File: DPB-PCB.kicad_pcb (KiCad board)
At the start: 4 copper layers, 86.6 x 60 mm, 98 parts, among them J1 USB_C_Prog, J2 LCD_Conn, J3 IMU_FFC_Conn, J4 IR_SENSOR, J5 ESC_Conn, J6 IR_LED, J7 XT60 - M, J8 USB_C_OTG, Q1 AO3401A, Q2 MMBT5551, Q3 MMBT5551, U1 ESP32-S3-WROOM-1-N4R2, U2 RT7272BGSP, U3 AMS1117-3.3, U4 USBLC6-4SC6, U5 CP2102N-Axx-xQFN28, U6 USBLC6-4SC6, U7 LM358

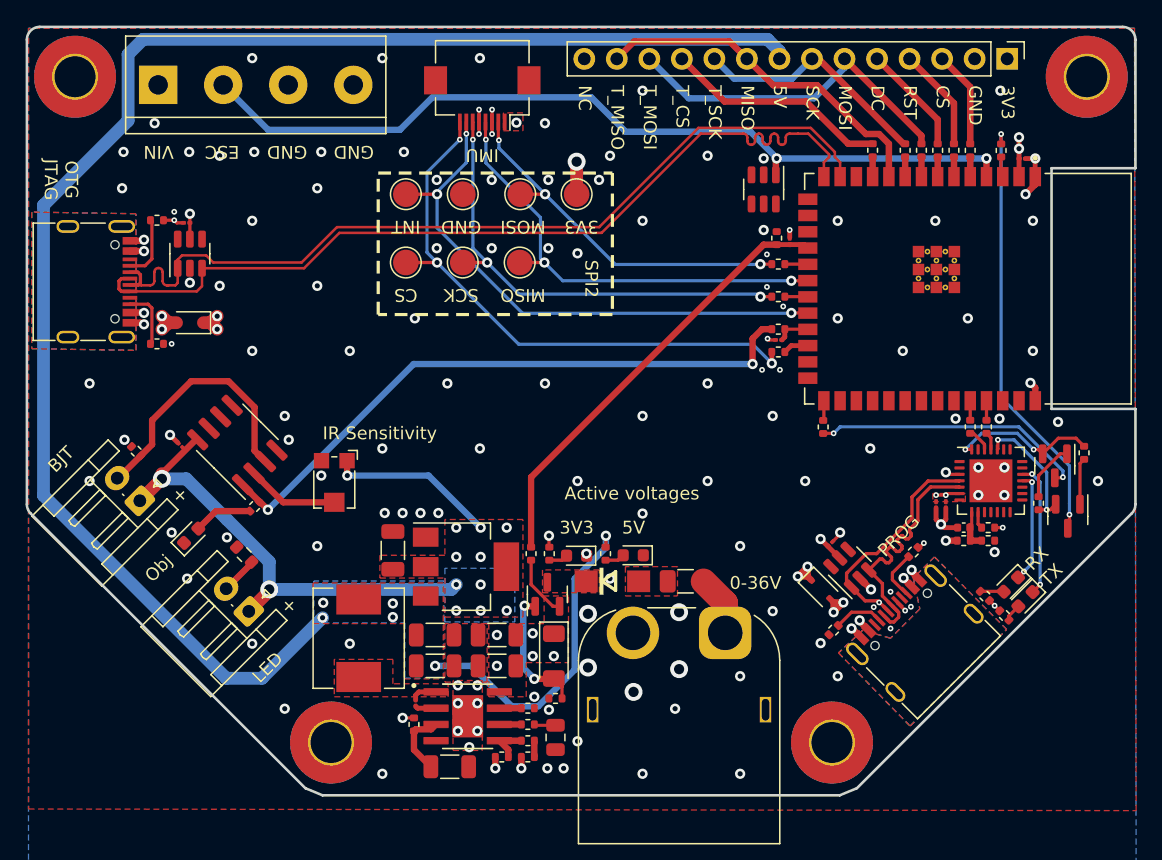
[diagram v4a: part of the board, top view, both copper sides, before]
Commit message: Align mech holed
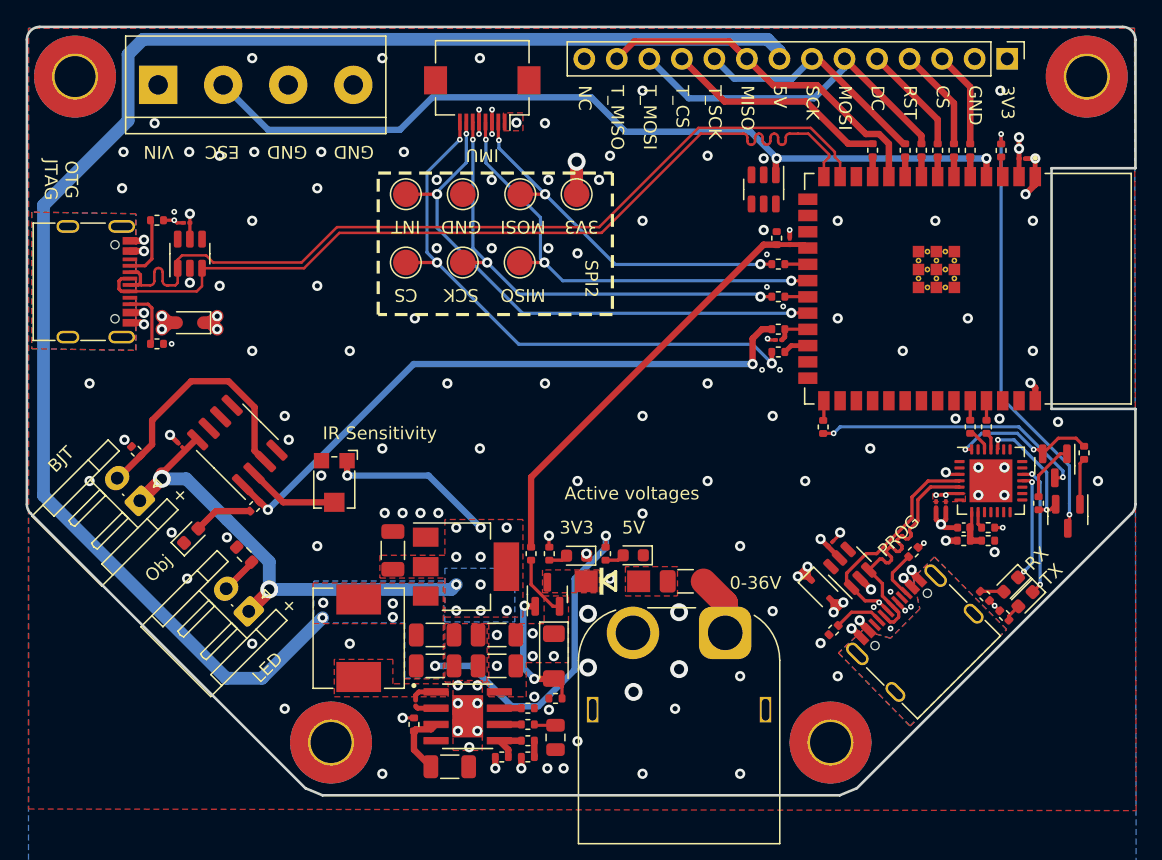
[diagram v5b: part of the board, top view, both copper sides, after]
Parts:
- moved H2 0.12 mm to (163.0, 134.0)
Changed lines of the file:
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@@
       (layer "F.SilkS" (type "Top Silk Screen") (color "White"))
       (layer "F.Paste" (type "Top Solder Paste"))
-      (layer "F.Mask" (type "Top Solder Mask") (color "Black") (thickness 0.01))
+      (layer "F.Mask" (type "Top Solder Mask") (color "Blue") (thickness 0.01))
       (layer "F.Cu" (type "copper") (thickness 0.035))
-      (layer "dielectric 1" (type "prepreg") (thickness 0.2104) (material "FR4") (epsilon_r 4.5) (loss_tangent 0.02))
+      (layer "dielectric 1" (type "prepreg") (color "FR4 natural") (thickness 0.2104) (material "FR4") (epsilon_r 4.5) (loss_tangent 0.02))
       (layer "In1.Cu" (type "copper") (thickness 0.0152))
-      (layer "dielectric 2" (type "core") (thickness 1.065) (material "FR4") (epsilon_r 4.5) (loss_tangent 0.02))
+      (layer "dielectric 2" (type "core") (color "Polyimide") (thickness 1.065) (material "FR4") (epsilon_r 4.5) (loss_tangent 0.02))
       (layer "In2.Cu" (type "copper") (thickness 0.0152))
-      (layer "dielectric 3" (type "prepreg") (thickness 0.2104) (material "FR4") (epsilon_r 4.5) (loss_tangent 0.02))
+      (layer "dielectric 3" (type "prepreg") (color "FR4 natural") (thickness 0.2104) (material "FR4") (epsilon_r 4.5) (loss_tangent 0.02))
       (layer "B.Cu" (type "copper") (thickness 0.035))
-      (layer "B.Mask" (type "Bottom Solder Mask") (color "Black") (thickness 0.01))
+      (layer "B.Mask" (type "Bottom Solder Mask") (color "Blue") (thickness 0.01))
       (layer "B.Paste" (type "Bottom Solder Paste"))
       (layer "B.SilkS" (type "Bottom Silk Screen") (color "White"))
@@
   )
   (footprint "MountingHole:MountingHole_3.2mm_M3_Pad_TopBottom" (layer "F.Cu")
-    (at 182.962 82.013)
+    (at 182.962 82)
     (descr "Mounting Hole 3.2mm, M3")
     (tags "mounting hole 3.2mm m3")
@@
   )
   (footprint "MountingHole:MountingHole_3.2mm_M3_Pad_TopBottom" (layer "F.Cu")
-    (at 103.962 82.013)
+    (at 103.962 82)
     (descr "Mounting Hole 3.2mm, M3")
     (tags "mounting hole 3.2mm m3")
@@
   )
   (footprint "MountingHole:MountingHole_3.2mm_M3_Pad_TopBottom" (layer "F.Cu")
-    (at 163.068 134)
+    (at 162.952 134)
     (descr "Mounting Hole 3.2mm, M3")
     (tags "mounting hole 3.2mm m3")

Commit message: On production | V0.1
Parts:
- added 3V2: ~, TestPoint:TestPoint_Pad_D2.0mm, F.Cu at (106.4, 71.7)
- added C18: 100n 50V, Capacitor_SMD:C_01005_0402Metric, F.Cu at (119.3, 56.7)
- added C19: 100n 50V, Capacitor_SMD:C_01005_0402Metric, F.Cu at (116.9, 57.7)
- added CS2: ~, TestPoint:TestPoint_Pad_D2.0mm, F.Cu at (127.7, 71.7)
- added D11: LED_GREEN, LED_SMD:LED_0603_1608Metric, F.Cu at (107.2, 67.2)
- added D12: SMF05CT1G, Package_TO_SOT_SMD:SOT-23-6, F.Cu at (117.2, 60.2)
- added GND2: ~, TestPoint:TestPoint_Pad_D2.0mm, F.Cu at (113.6, 71.7)
- added H5: M3, MountingHole:MountingHole_3.2mm_M3_Pad_TopBottom, F.Cu at (105.7, 59.2)
- added H6: M3, MountingHole:MountingHole_3.2mm_M3_Pad_TopBottom, F.Cu at (128.7, 59.2)
- added INT2: ~, TestPoint:TestPoint_Pad_D2.0mm, F.Cu at (124.2, 71.6)
- added J9: IMU_FFC_Conn, Connector_FFC-FPC:Hirose_FH12-8S-0.5SH_1x08-1MP_P0.50mm_Horizontal, F.Cu at (117.2, 65.1)
- added MISO2: ~, TestPoint:TestPoint_Pad_D2.0mm, F.Cu at (117.1, 71.7)
- added MOSI2: ~, TestPoint:TestPoint_Pad_D2.0mm, F.Cu at (110.0, 71.7)
- added R40: 1k, Resistor_SMD:R_0402_1005Metric, F.Cu at (105.9, 67.7)
- added R41: 47, Resistor_SMD:R_0402_1005Metric, F.Cu at (114.8, 55.1)
- added R42: 47, Resistor_SMD:R_0402_1005Metric, F.Cu at (115.3, 57.8)
- added SCK2: ~, TestPoint:TestPoint_Pad_D2.0mm, F.Cu at (120.6, 71.7)
- added Ue: LSM6DSLTR, Library:PQFN50P300X250X86-14N, F.Cu at (117.2, 55.8)
- added mouse-bite-2.54mm-slot: VAL**, Library:mouse-bite-2.54mm-slot, F.Cu at (105.0, 76.9)
- added mouse-bite-2.54mm-slot1: VAL**, Library:mouse-bite-2.54mm-slot, F.Cu at (116.8, 76.9)
- added mouse-bite-2.54mm-slot2: VAL**, Library:mouse-bite-2.54mm-slot, F.Cu at (128.8, 76.9)
- renumbered R38 to R31, R39 to R32, R31 to R33, R32 to R34, R33 to R35, R34 to R36, R35 to R37, R36 to R38, R37 to R39
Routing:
- net /IMU/CS: track 0.00 -> 30.6 mm, vias 0 -> 3
- net /IMU/MOSi: track 0.00 -> 26.5 mm, vias 0 -> 4
- net /IMU/SCK: track 0.00 -> 24.9 mm, vias 0 -> 4
- net /IMU/MISO: track 0.00 -> 21.4 mm, vias 0 -> 4
- net /IMU/INT1: track 0.00 -> 21.0 mm, vias 0 -> 3
- net GND2: track 0.00 -> 10.9 mm, vias 0 -> 40
- net /IMU/3V3: track 0.00 -> 5.20 mm, vias 0 -> 12
- net Net-(D11-A): track 0.00 -> 1.44 mm
- net Net-(U8-INT1): track 0.00 -> 1.43 mm
- net Net-(U8-SDO/SA0): track 0.00 -> 1.34 mm
- net Earth_Protective: vias 0 -> 42
- added copper zone on F.Cu, net /IMU/3V3
- added copper zone on In2.Cu, net /IMU/3V3
- added copper zone on B.Cu, net Earth_Protective
- added copper zone on F.Cu, net Earth_Protective
- added copper zone on In1.Cu, net Earth_Protective
- added copper zone on In2.Cu, net Earth_Protective
- added copper zone on B.Cu, net GND2
- added copper zone on F.Cu, net GND2
- added copper zone on In1.Cu, net GND2
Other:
- board size 86.6 x 60 mm -> 86.6 x 86.5 mm
- rule pad_to_mask_clearance: 0.05 -> 0
- board text added: "DPB"
- board text added: "INT1"
- board text added: "LSM6DS 3TR-C"
- board text added: "PWR"
- board text added: "X"
- board text added: "Y"
- board text added: "®"
- board text added: "¯"
- board text added: "·"

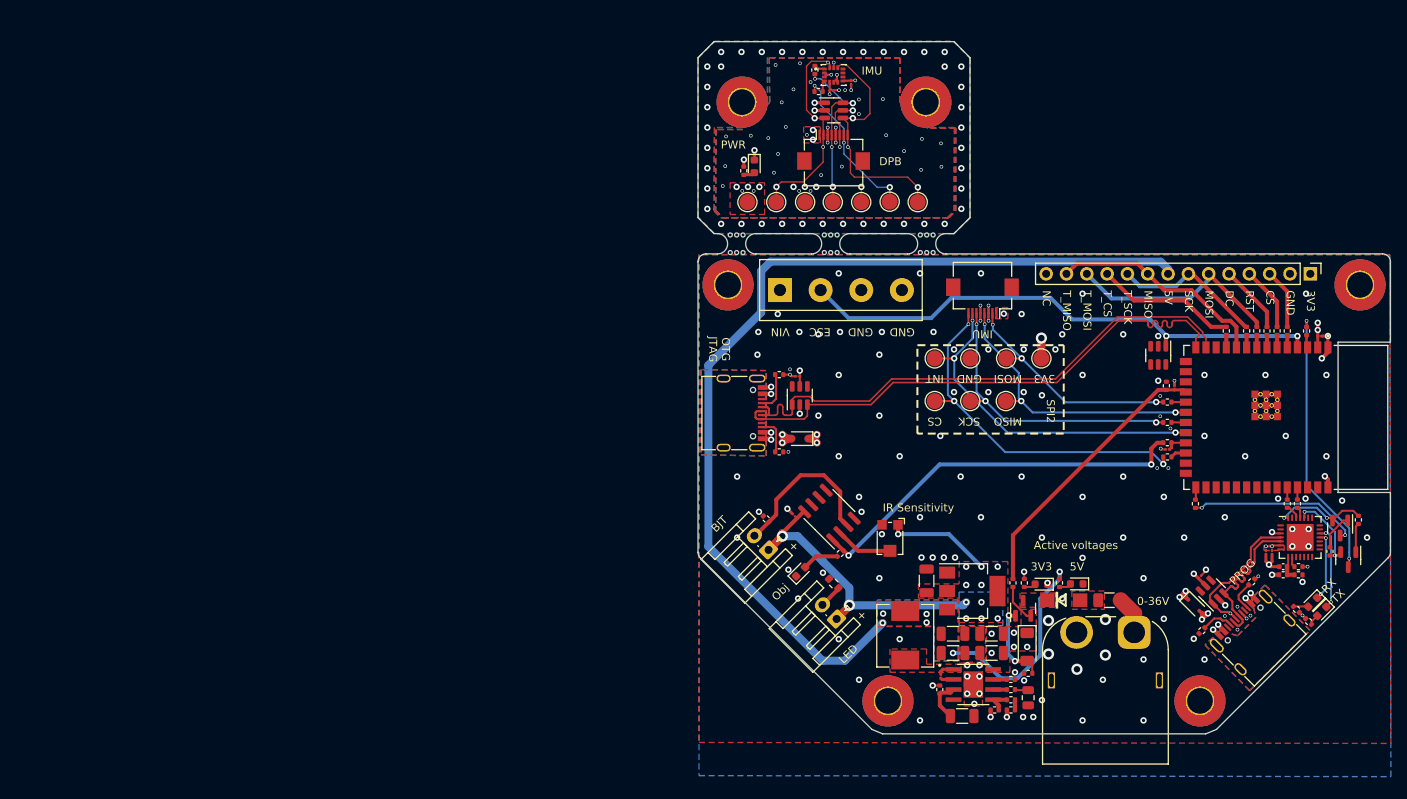
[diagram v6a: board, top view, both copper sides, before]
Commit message: Edge cut changed to avoid supplement fee
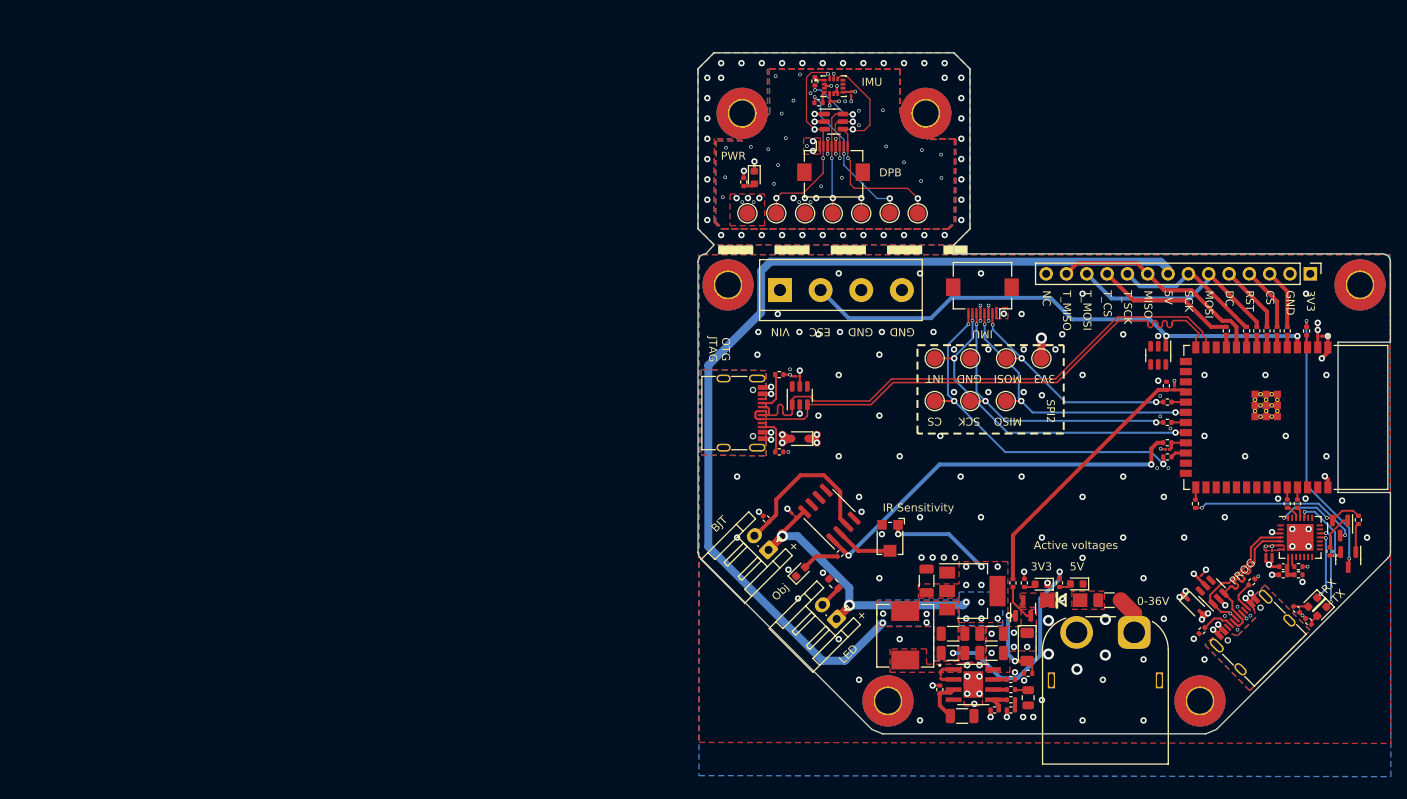
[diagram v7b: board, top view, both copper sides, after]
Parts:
- removed mouse-bite-2.54mm-slot, mouse-bite-2.54mm-slot1, mouse-bite-2.54mm-slot2: VAL**, Library:mouse-bite-2.54mm-slot
- moved D11 1.40 mm to (107.2, 68.6)
- moved H5 1.40 mm to (105.7, 60.6)
- moved H6 1.40 mm to (128.7, 60.6)
- moved INT2 1.40 mm to (124.2, 73.0)
- moved J9 1.40 mm to (117.2, 66.5)
- moved R40 1.40 mm to (105.9, 69.1)
- moved R41 1.40 mm to (114.8, 56.5)
- moved C18 1.40 mm to (119.3, 58.1)
- moved C19 1.40 mm to (116.9, 59.1)
- moved D12 1.40 mm to (117.2, 61.6)
- moved R42 1.40 mm to (115.3, 59.2)
- moved Ue 1.40 mm to (117.2, 57.2)
- moved 3V2 1.40 mm to (106.4, 73.1)
- moved CS2 1.40 mm to (127.7, 73.1)
- moved GND2 1.40 mm to (113.6, 73.1)
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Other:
- board size 86.6 x 86.5 mm -> 86.6 x 85.1 mm

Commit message: Add hysteresis to IR sensor. Update README file.
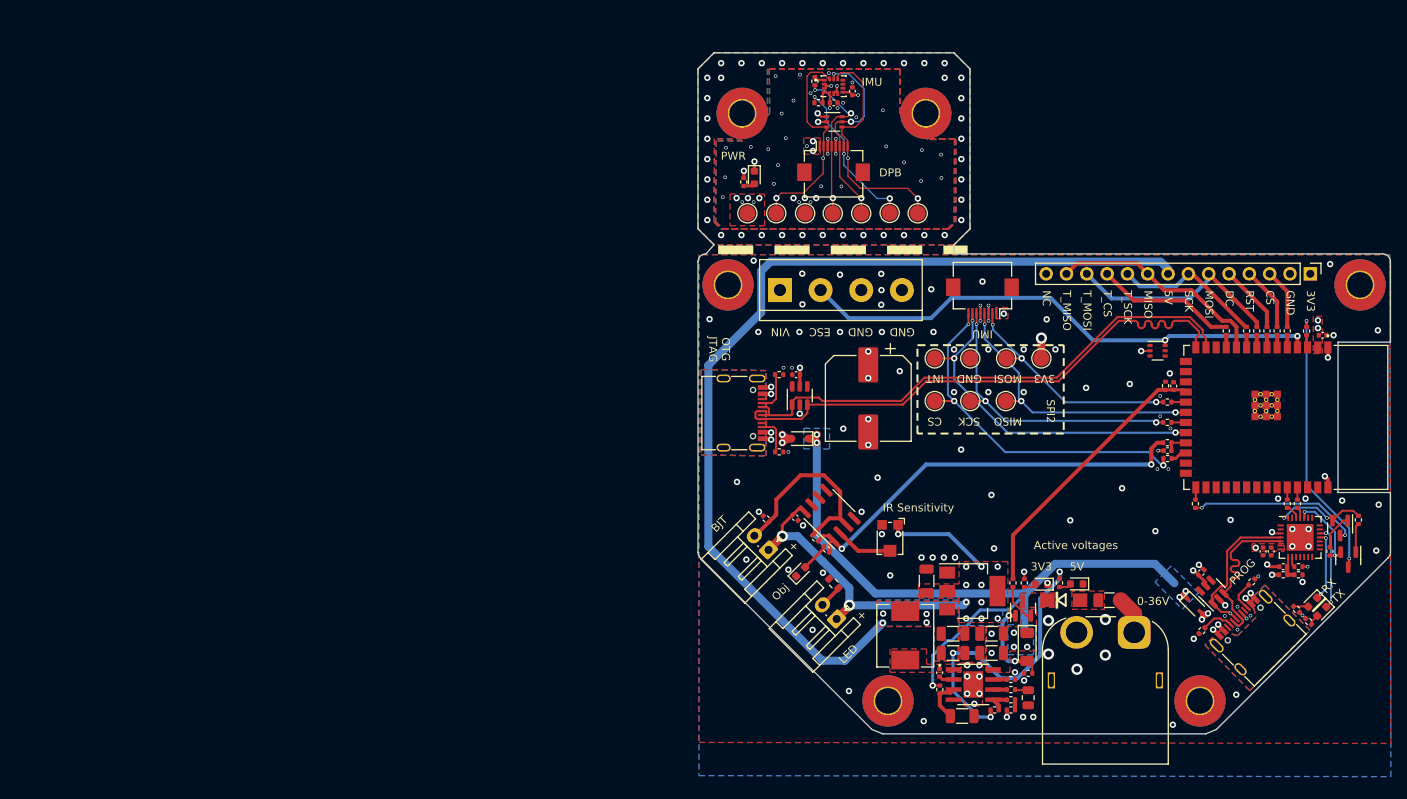
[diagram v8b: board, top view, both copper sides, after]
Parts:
- added C21: 470uf 35V, Capacitor_SMD:CP_Elec_10x14.3, F.Cu at (121.5, 96.2)
- added R43: 100k, Resistor_SMD:R_0402_1005Metric, F.Cu at (114.9, 113.6)
- C1, C12, C13, C14, C15, C16, C17, C18, C19, C2, C7: footprint Capacitor_SMD:C_01005_0402Metric -> Capacitor_SMD:C_0402_1005Metric
- D12, D9: footprint Package_TO_SOT_SMD:SOT-23-6 -> Package_TO_SOT_SMD:SOT-363_SC-70-6
- moved R38 1.78 mm to (116.3, 115.0), turned to -45 degrees
- moved D9 0.59 mm to (157.6, 90.2), turned to 0 degrees
- moved C12 0.56 mm to (163.1, 118.0)
- moved C7 0.46 mm to (130.4, 130.5)
- moved C14 0.38 mm to (170.8, 115.3)
- moved C1 0.37 mm to (178.3, 88.3)
- moved C16 0.35 mm to (112.4, 111.1), turned to -45 degrees
- moved C18 0.35 mm to (119.5, 57.8), turned to 90 degrees
- moved C15 0.29 mm to (112.5, 93.2)
- moved C19 0.27 mm to (117.2, 59.2)
- moved C2 0.25 mm to (159.7, 94.6)
- moved R9 0.20 mm to (158.9, 103.7)
- moved C13 0.16 mm to (171.9, 115.3)
- moved C17 0.15 mm to (158.9, 102.7)
- moved R12 0.10 mm to (158.6, 94.6)
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- renumbered Ue to U8
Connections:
- D9 pad 1: ESC_CMD -> unconnected-(D9-K-Pad1)
- D9 pad 6: unconnected-(D9-K-Pad6) -> ESC_CMD
- J5 pad 1: VCC -> +VDC
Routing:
- net VCC: track 12.4 -> 95.8 mm
- net GND: track 26.7 -> 19.4 mm, vias 140 -> 118
- net IR_SENSE_A: track 20.4 -> 26.0 mm
- net +3.3V: track 60.5 -> 56.4 mm, vias 22 -> 21
- net Net-(R38-Pad2): track 49.2 -> 52.4 mm
- net USB_D-: track 69.1 -> 66.9 mm
- net /Power Supply/SW: track 2.06 -> 0.00 mm
- net GND2: track 10.9 -> 9.36 mm
- net /USB/D+: track 21.3 -> 22.4 mm
- net /USB/D-: track 20.2 -> 21.2 mm
- net Net-(D4-A): track 10.3 -> 11.4 mm
- net Net-(D10-A): track 4.60 -> 3.59 mm
- net /IMU/3V3: track 5.20 -> 6.04 mm
- net /IMU/MISO: track 21.4 -> 20.8 mm, vias 4 -> 3
- net /IMU/CS: track 30.6 -> 30.1 mm, vias 3 -> 2
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- added copper zone on In2.Cu, net +VDC
- added copper zone on B.Cu, net VCC
- removed copper zone on In2.Cu, net VCC
- removed copper zone on In2.Cu, net unconnected-(J1-SHIELD-PadS1)
- removed copper zone on In2.Cu, net unconnected-(J8-SHIELD-PadS1)
